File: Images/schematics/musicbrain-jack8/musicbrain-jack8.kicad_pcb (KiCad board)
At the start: 2 copper layers, 20 x 125 mm, 10 parts, among them J1 SOCKET-BACK, J2 PJ398SM, J3 PJ398SM, J4 PJ398SM, J5 PJ398SM, J6 PJ398SM, J7 PJ398SM, J8 PJ398SM, J9 PJ398SM

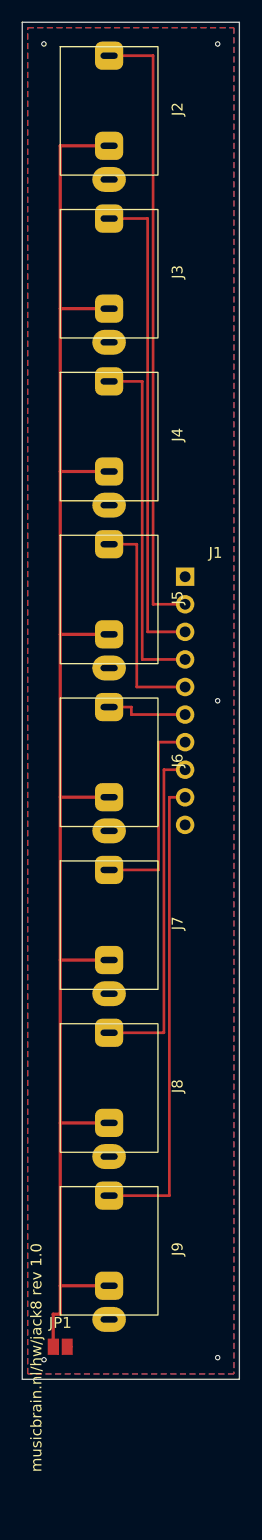
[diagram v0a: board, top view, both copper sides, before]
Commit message: jack8/jack4 v1.1: socket naar de achterzijde + netnaam-fix
De 1xN female socket (J1) stond als footprint op F.Cu waardoor hij in de
3D-render (en assembly!) bovenop naast de jacks belandde; nu correct op
B.Cu met gespiegelde silk/courtyard en geflipt 3D-model - opening omlaag,
naar de kaart. Jack-hartlijn blijft 8,0mm van de westrand: dat wordt de
uitlijn-standaard voor alle front-borden (pots op dezelfde lijn). Bonus:
NORM-net heette in de PCB anders dan in het schema (netcheck ving dat nu).
ERC 0, netcheck OK, DRC 0/0, fab-pakketten ververst (JLC-formaat).

Co-Authored-By: Claude Fable 5 <noreply@anthropic.com>
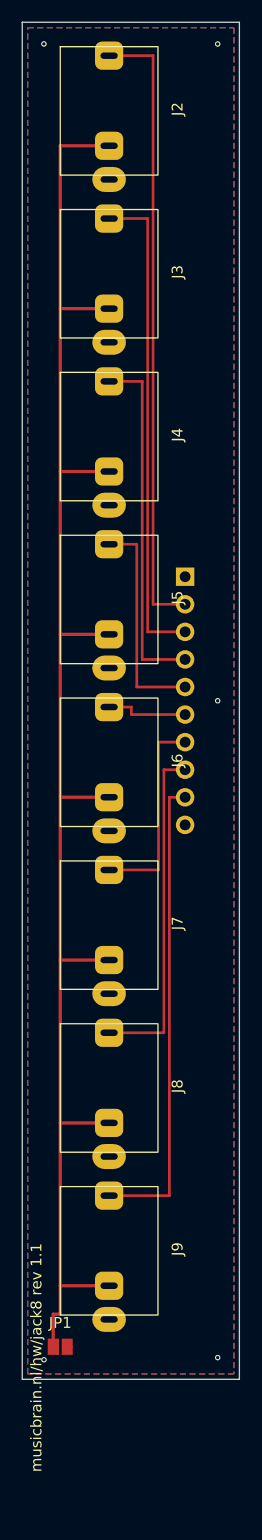
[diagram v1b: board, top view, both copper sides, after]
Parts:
- J1: moved to B.Cu
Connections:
- net NORM renamed /NORM
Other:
- board text added: "musicbrain.nl/hw/jack8 rev 1.1"
- board text removed: "musicbrain.nl/hw/jack8 rev 1.0"
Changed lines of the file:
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@@
     (title "MusicBrain jack8")
     (date "2026-07-08")
-    (rev "1.0")
+    (rev "1.1")
     (company "MusicBrain project")
   )
@@
   (net 0 "")
   (net 1 "GND")
-  (net 2 "NORM")
+  (net 2 "/NORM")
   (net 3 "/CH1")
   (net 4 "/CH2")
@@
     (pad "1" thru_hole roundrect (at 0 -4.92) (size 2.6 2.6) (drill oval 1.6 0.6) (layers "*.Cu" "*.Mask") (roundrect_rratio 0.25) (net 3 "/CH1"))
     (pad "2" thru_hole oval (at 0 6.48) (size 3.1 2.3) (drill oval 1.6 0.6) (layers "*.Cu" "*.Mask") (net 1 "GND"))
-    (pad "3" thru_hole roundrect (at 0 3.38) (size 2.6 2.6) (drill oval 1.6 0.6) (layers "*.Cu" "*.Mask") (roundrect_rratio 0.25) (net 2 "NORM"))
+    (pad "3" thru_hole roundrect (at 0 3.38) (size 2.6 2.6) (drill oval 1.6 0.6) (layers "*.Cu" "*.Mask") (roundrect_rratio 0.25) (net 2 "/NORM"))
     (model "${KIPRJMOD}/../3d/PJ301M-12_Thonkiconn.stp"
       (offset (xyz 0 0.75 0)) (scale (xyz 1 1 1)) (rotate (xyz 0 0 0)))
@@
     (pad "1" thru_hole roundrect (at 0 -4.92) (size 2.6 2.6) (drill oval 1.6 0.6) (layers "*.Cu" "*.Mask") (roundrect_rratio 0.25) (net 4 "/CH2"))
     (pad "2" thru_hole oval (at 0 6.48) (size 3.1 2.3) (drill oval 1.6 0.6) (layers "*.Cu" "*.Mask") (net 1 "GND"))
-    (pad "3" thru_hole roundrect (at 0 3.38) (size 2.6 2.6) (drill oval 1.6 0.6) (layers "*.Cu" "*.Mask") (roundrect_rratio 0.25) (net 2 "NORM"))
+    (pad "3" thru_hole roundrect (at 0 3.38) (size 2.6 2.6) (drill oval 1.6 0.6) (layers "*.Cu" "*.Mask") (roundrect_rratio 0.25) (net 2 "/NORM"))
     (model "${KIPRJMOD}/../3d/PJ301M-12_Thonkiconn.stp"
       (offset (xyz 0 0.75 0)) (scale (xyz 1 1 1)) (rotate (xyz 0 0 0)))
@@
     (pad "1" thru_hole roundrect (at 0 -4.92) (size 2.6 2.6) (drill oval 1.6 0.6) (layers "*.Cu" "*.Mask") (roundrect_rratio 0.25) (net 5 "/CH3"))
     (pad "2" thru_hole oval (at 0 6.48) (size 3.1 2.3) (drill oval 1.6 0.6) (layers "*.Cu" "*.Mask") (net 1 "GND"))
-    (pad "3" thru_hole roundrect (at 0 3.38) (size 2.6 2.6) (drill oval 1.6 0.6) (layers "*.Cu" "*.Mask") (roundrect_rratio 0.25) (net 2 "NORM"))
+    (pad "3" thru_hole roundrect (at 0 3.38) (size 2.6 2.6) (drill oval 1.6 0.6) (layers "*.Cu" "*.Mask") (roundrect_rratio 0.25) (net 2 "/NORM"))
     (model "${KIPRJMOD}/../3d/PJ301M-12_Thonkiconn.stp"
       (offset (xyz 0 0.75 0)) (scale (xyz 1 1 1)) (rotate (xyz 0 0 0)))
@@
     (pad "1" thru_hole roundrect (at 0 -4.92) (size 2.6 2.6) (drill oval 1.6 0.6) (layers "*.Cu" "*.Mask") (roundrect_rratio 0.25) (net 6 "/CH4"))
     (pad "2" thru_hole oval (at 0 6.48) (size 3.1 2.3) (drill oval 1.6 0.6) (layers "*.Cu" "*.Mask") (net 1 "GND"))
-    (pad "3" thru_hole roundrect (at 0 3.38) (size 2.6 2.6) (drill oval 1.6 0.6) (layers "*.Cu" "*.Mask") (roundrect_rratio 0.25) (net 2 "NORM"))
+    (pad "3" thru_hole roundrect (at 0 3.38) (size 2.6 2.6) (drill oval 1.6 0.6) (layers "*.Cu" "*.Mask") (roundrect_rratio 0.25) (net 2 "/NORM"))
     (model "${KIPRJMOD}/../3d/PJ301M-12_Thonkiconn.stp"
       (offset (xyz 0 0.75 0)) (scale (xyz 1 1 1)) (rotate (xyz 0 0 0)))
@@
     (pad "1" thru_hole roundrect (at 0 -4.92) (size 2.6 2.6) (drill oval 1.6 0.6) (layers "*.Cu" "*.Mask") (roundrect_rratio 0.25) (net 7 "/CH5"))
     (pad "2" thru_hole oval (at 0 6.48) (size 3.1 2.3) (drill oval 1.6 0.6) (layers "*.Cu" "*.Mask") (net 1 "GND"))
-    (pad "3" thru_hole roundrect (at 0 3.38) (size 2.6 2.6) (drill oval 1.6 0.6) (layers "*.Cu" "*.Mask") (roundrect_rratio 0.25) (net 2 "NORM"))
+    (pad "3" thru_hole roundrect (at 0 3.38) (size 2.6 2.6) (drill oval 1.6 0.6) (layers "*.Cu" "*.Mask") (roundrect_rratio 0.25) (net 2 "/NORM"))
     (model "${KIPRJMOD}/../3d/PJ301M-12_Thonkiconn.stp"
       (offset (xyz 0 0.75 0)) (scale (xyz 1 1 1)) (rotate (xyz 0 0 0)))
@@
     (pad "1" thru_hole roundrect (at 0 -4.92) (size 2.6 2.6) (drill oval 1.6 0.6) (layers "*.Cu" "*.Mask") (roundrect_rratio 0.25) (net 8 "/CH6"))
     (pad "2" thru_hole oval (at 0 6.48) (size 3.1 2.3) (drill oval 1.6 0.6) (layers "*.Cu" "*.Mask") (net 1 "GND"))
-    (pad "3" thru_hole roundrect (at 0 3.38) (size 2.6 2.6) (drill oval 1.6 0.6) (layers "*.Cu" "*.Mask") (roundrect_rratio 0.25) (net 2 "NORM"))
+    (pad "3" thru_hole roundrect (at 0 3.38) (size 2.6 2.6) (drill oval 1.6 0.6) (layers "*.Cu" "*.Mask") (roundrect_rratio 0.25) (net 2 "/NORM"))
     (model "${KIPRJMOD}/../3d/PJ301M-12_Thonkiconn.stp"
       (offset (xyz 0 0.75 0)) (scale (xyz 1 1 1)) (rotate (xyz 0 0 0)))
@@
     (pad "1" thru_hole roundrect (at 0 -4.92) (size 2.6 2.6) (drill oval 1.6 0.6) (layers "*.Cu" "*.Mask") (roundrect_rratio 0.25) (net 9 "/CH7"))
     (pad "2" thru_hole oval (at 0 6.48) (size 3.1 2.3) (drill oval 1.6 0.6) (layers "*.Cu" "*.Mask") (net 1 "GND"))
-    (pad "3" thru_hole roundrect (at 0 3.38) (size 2.6 2.6) (drill oval 1.6 0.6) (layers "*.Cu" "*.Mask") (roundrect_rratio 0.25) (net 2 "NORM"))
+    (pad "3" thru_hole roundrect (at 0 3.38) (size 2.6 2.6) (drill oval 1.6 0.6) (layers "*.Cu" "*.Mask") (roundrect_rratio 0.25) (net 2 "/NORM"))
     (model "${KIPRJMOD}/../3d/PJ301M-12_Thonkiconn.stp"
       (offset (xyz 0 0.75 0)) (scale (xyz 1 1 1)) (rotate (xyz 0 0 0)))
@@
     (pad "1" thru_hole roundrect (at 0 -4.92) (size 2.6 2.6) (drill oval 1.6 0.6) (layers "*.Cu" "*.Mask") (roundrect_rratio 0.25) (net 10 "/CH8"))
     (pad "2" thru_hole oval (at 0 6.48) (size 3.1 2.3) (drill oval 1.6 0.6) (layers "*.Cu" "*.Mask") (net 1 "GND"))
-    (pad "3" thru_hole roundrect (at 0 3.38) (size 2.6 2.6) (drill oval 1.6 0.6) (layers "*.Cu" "*.Mask") (roundrect_rratio 0.25) (net 2 "NORM"))
+    (pad "3" thru_hole roundrect (at 0 3.38) (size 2.6 2.6) (drill oval 1.6 0.6) (layers "*.Cu" "*.Mask") (roundrect_rratio 0.25) (net 2 "/NORM"))
     (model "${KIPRJMOD}/../3d/PJ301M-12_Thonkiconn.stp"
       (offset (xyz 0 0.75 0)) (scale (xyz 1 1 1)) (rotate (xyz 0 0 0)))
   )
   (footprint "MusicBrain:Header_1x10_backside"
-    (layer "F.Cu")
+    (layer "B.Cu")
     (at 115 151.07)
-    (descr "1x10 female socket - OP ACHTERZIJDE monteren (opening naar de kaart)")
-    (property "Reference" "J1" (at 2.8 -2.2 0) (layer "F.SilkS")
-      (effects (font (size 1 1) (thickness 0.15))))
-    (property "Value" "SOCKET-BACK" (at 0 25.86 0) (layer "F.Fab")
-      (effects (font (size 1 1) (thickness 0.15))))
+    (descr "1x10 female socket op de ACHTERZIJDE (opening omlaag, naar de kaart)")
+    (property "Reference" "J1" (at 2.8 -2.2 0) (layer "B.SilkS")
+      (effects (font (size 1 1) (thickness 0.15)) (justify mirror)))
+    (property "Value" "SOCKET-BACK" (at 0 25.86 0) (layer "B.Fab")
+      (effects (font (size 1 1) (thickness 0.15)) (justify mirror)))
     (attr through_hole)
     (fp_rect (start -1.6 -1.6) (end 1.6 24.46)
       (stroke (width 0.12) (type solid)) (fill no) (layer "B.SilkS"))
     (fp_rect (start -1.8 -1.8) (end 1.8 24.66)
-      (stroke (width 0.05) (type solid)) (fill no) (layer "F.CrtYd"))
+      (stroke (width 0.05) (type solid)) (fill no) (layer "B.CrtYd"))
     (pad "1" thru_hole rect (at 0 0) (size 1.7 1.7) (drill 1.0) (layers "*.Cu" "*.Mask") (net 1 "GND"))
     (pad "2" thru_hole oval (at 0 2.54) (size 1.7 1.7) (drill 1.0) (layers "*.Cu" "*.Mask") (net 3 "/CH1"))
@@
     (pad "10" thru_hole oval (at 0 22.86) (size 1.7 1.7) (drill 1.0) (layers "*.Cu" "*.Mask") (net 1 "GND"))
     (model "${KICAD10_3DMODEL_DIR}/Connector_PinSocket_2.54mm.3dshapes/PinSocket_1x10_P2.54mm_Vertical.step"
-      (offset (xyz 0 11.43 0)) (scale (xyz 1 1 1)) (rotate (xyz 0 0 0)))
+      (offset (xyz 0 11.43 -1.6)) (scale (xyz 1 1 1)) (rotate (xyz 180 0 0)))
   )
   (footprint "Jumper:SolderJumper-2_P1.3mm_Open_TrianglePad1.0x1.5mm"
@@
       (options (clearance outline) (anchor rect))
       (primitives (gr_poly (pts (xy 0.5 0.75) (xy 0.5 -0.75) (xy -0.5 0) ) (width 0) (fill yes)))
-      (net 2 "NORM"))
+      (net 2 "/NORM"))
     (pad "2" smd custom (at 0.65 0) (size 1 1.5) (layers "F.Cu" "F.Mask")
       (options (clearance outline) (anchor rect))
@@
     (stroke (width 0.1) (type default)) (fill none)
     (layer "Edge.Cuts"))
-  (gr_text "musicbrain.nl/hw/jack8 rev 1.0" (at 101.3 223 90) (layer "F.SilkS")
+  (gr_text "musicbrain.nl/hw/jack8 rev 1.1" (at 101.3 223 90) (layer "F.SilkS")
     (effects (font (size 1 1) (thickness 0.15))))
   (zone (net 1) (net_name "GND") (layer "F.Cu")
